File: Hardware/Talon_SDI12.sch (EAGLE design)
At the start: 123 parts, among them J1 CONN_APOGEE_LOGGER, J2 CONN_TALON_REMOTE, J3 CONN_SDI-12_LOGGERM8_TE_BOARD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, J4 CONN_SDI-12_LOGGERM8_TE_BOARD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, J5 CONN_SDI-12_LOGGERM8_TE_BOARD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, Q1 2N7002, Q2 2N7002, Q3 2N7002, Q4 2N7002, Q5 AO3419, Q6 AO3419, Q7 AO3419, Q8 AO3419, U1 SN74HC04, U10 FXMAR2102UMLP, U11 74HC4852, U12 SN74LVC1G3157SC70, U13 MCP3221, U14 MCP23018QFN, U15 PCA9536DFN, U16 MCP3421A3, U17 SN74LVC1G3157SC70, U18 SN74LVC1G3157SC70, U19 SN74LVC1G3157SC70, U2 CD4044, U20 SN74LVC1G3157SC70, U21 SN74LVC1G00SC70, U22 SN74LVC2G241DCU, U23 SN74LVC1G17DCK, U24 24AA02SOT23, U3 SIP32431TDFN, U4 INA4180A2, U5 MAX9034TSSOP, U6 SI1869, U7 SN74AC08, U8 LM2621, U9 LMR62014SOT23

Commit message: Updated EEPROM part number
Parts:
- D10, D11, D8, D9: value 5.1V -> (none)
- U24: value 24AA02SOT23 -> AT24MAC602SOT23; device bschulz:24AA02SOT23 -> bschulz:AT24MAC602SOT23
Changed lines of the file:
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@@
 </part>
 <part name="GND57" library="supply1" library_urn="urn:adsk.eagle:library:371" deviceset="GND" device=""/>
-<part name="U24" library="bschulz" deviceset="24AA02" device="SOT23"/>
+<part name="U24" library="bschulz" deviceset="AT24MAC*02" device="SOT23" technology="6" value="AT24MAC602SOT23"/>
 <part name="GND58" library="supply1" library_urn="urn:adsk.eagle:library:371" deviceset="GND" device=""/>
 <part name="R31" library="bschulz_passives" deviceset="R-EU_" device="R0402" technology="1K" value="1k"/>
@@
 <part name="R41" library="bschulz_passives" deviceset="R-EU_" device="R0402" technology="510" value="510R"/>
 <part name="GND62" library="supply1" library_urn="urn:adsk.eagle:library:371" deviceset="GND" device=""/>
-<part name="D8" library="bschulz" deviceset="DIODE_ZENER" device="SOD-323" value="5.1V">
+<part name="D8" library="bschulz" deviceset="DIODE_ZENER" device="SOD-323">
 <attribute name="DIGIKEY" value="BZX384B5V1-HE3-08GICT-ND"/>
 <attribute name="MF" value="Vishay"/>
@@
 <part name="GND63" library="supply1" library_urn="urn:adsk.eagle:library:371" deviceset="GND" device=""/>
 <part name="R42" library="bschulz_passives" deviceset="R-EU_" device="R0402" technology="510" value="510R"/>
-<part name="D9" library="bschulz" deviceset="DIODE_ZENER" device="SOD-323" value="5.1V">
+<part name="D9" library="bschulz" deviceset="DIODE_ZENER" device="SOD-323">
 <attribute name="DIGIKEY" value="BZX384B5V1-HE3-08GICT-ND"/>
 <attribute name="MF" value="Vishay"/>
@@
 <part name="GND64" library="supply1" library_urn="urn:adsk.eagle:library:371" deviceset="GND" device=""/>
 <part name="R43" library="bschulz_passives" deviceset="R-EU_" device="R0402" technology="510" value="510R"/>
-<part name="D10" library="bschulz" deviceset="DIODE_ZENER" device="SOD-323" value="5.1V">
+<part name="D10" library="bschulz" deviceset="DIODE_ZENER" device="SOD-323">
 <attribute name="DIGIKEY" value="BZX384B5V1-HE3-08GICT-ND"/>
 <attribute name="MF" value="Vishay"/>
@@
 <part name="GND65" library="supply1" library_urn="urn:adsk.eagle:library:371" deviceset="GND" device=""/>
 <part name="R44" library="bschulz_passives" deviceset="R-EU_" device="R0402" technology="510" value="510R"/>
-<part name="D11" library="bschulz" deviceset="DIODE_ZENER" device="SOD-323" value="5.1V">
+<part name="D11" library="bschulz" deviceset="DIODE_ZENER" device="SOD-323">
 <attribute name="DIGIKEY" value="BZX384B5V1-HE3-08GICT-ND"/>
 <attribute name="MF" value="Vishay"/>

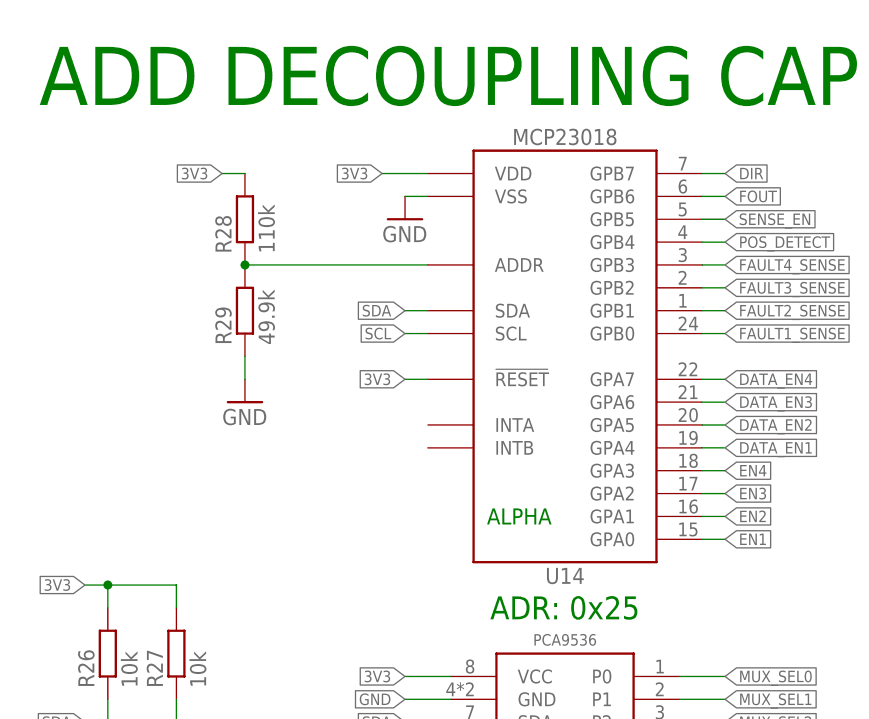
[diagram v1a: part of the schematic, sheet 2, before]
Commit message: Updated to v1.4
Added loopback functionality, replaced MCP23018 with PACL9535A, fixed inverter (U23) model, fixed attributes on schematics
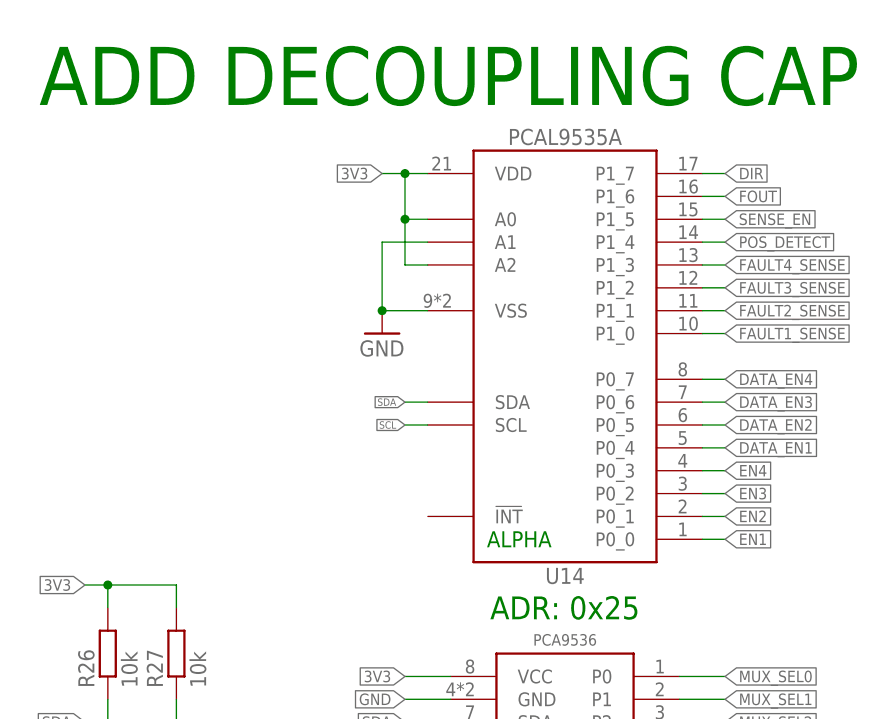
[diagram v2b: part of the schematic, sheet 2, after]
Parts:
- removed R28: 110k, bschulz_passives:R-EU_110KR0603
- removed R29: 49.9k, bschulz_passives:R-EU_49.9KR0603
- added U25: SN74AUP1T87, bschulz:SN74AUP1T87
- U14: value MCP23018QFN -> PCAL9535AQFN; device bschulz:MCP23018QFN -> bschulz:PCAL9535AQFN
- U23: value SN74LVC1G17DCK -> (none); device bschulz:SN74LVC1G17DCK -> bschulz:SN74LVC1G14DCK; DIGIKEY 296-11608-1-ND -> (none); DISP SN74LVC1G14 -> (none); MPN SN74LVC1G14DCKR -> (none)
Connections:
- removed net N$14: R28.1, R29.2, U14.ADDR
- new net DIR_BYPASS: U22.2OE, U25.Y
- net 3V3: now also U14.A0, U14.A2, U25.VCC; no longer R28.2, U14.!RESET
- net DATA_EN1: now also U14.P0_4; no longer U14.GPA4
- net DATA_EN2: now also U14.P0_5; no longer U14.GPA5
- net DATA_EN3: now also U14.P0_6; no longer U14.GPA6
- net DATA_EN4: now also U14.P0_7; no longer U14.GPA7
- net DIR: now also U14.P1_7, U25.A; no longer U14.GPB7, U22.2OE
- net EN1: now also U14.P0_0; no longer U14.GPA0
- net EN2: now also U14.P0_1; no longer U14.GPA1
- net EN3: now also U14.P0_2; no longer U14.GPA2
- net EN4: now also U14.P0_3; no longer U14.GPA3
- net FAULT1_SENSE: now also U14.P1_0; no longer U14.GPB0
- net FAULT2_SENSE: now also U14.P1_1; no longer U14.GPB1
- net FAULT3_SENSE: now also U14.P1_2; no longer U14.GPB2
- net FAULT4_SENSE: now also U14.P1_3; no longer U14.GPB3
- net FOUT: now also U14.P1_6; no longer U14.GPB6
- net GND: now also U14.A1, U25.GND; no longer R29.1
- net MUX_EN: now also U25.B
- net POS_DETECT: now also U14.P1_4; no longer U14.GPB4
- net SENSE_EN: now also U14.P1_5; no longer U14.GPB5
